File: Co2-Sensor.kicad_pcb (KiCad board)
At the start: 2 copper layers, 45 x 65 mm, 74 parts, among them J1 OLED, J2 SCD30, J3 LED, J4 Power, J5 USB_C_Receptacle_USB2.0, J6 LED, J7 SPS30, J8 I2C, Q1 S8050, Q2 S8050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

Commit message: Add changes for Rev. 2
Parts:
- removed D7: Red, LED_SMD:LED_0603_1608Metric
- removed R21: 0R NC, Resistor_SMD:R_0603_1608Metric
- removed R22: 0R, Resistor_SMD:R_0603_1608Metric
- added Q4: 2N7002, Package_TO_SOT_SMD:SOT-23, F.Cu at (163.0, 112.5)
- added REF**: MountingHole_JLCPCB, MountingHole:MountingHole_JLCPCB, F.Cu at (171.0, 128.0)
- added REF**: MountingHole_JLCPCB, MountingHole:MountingHole_JLCPCB, F.Cu at (129.0, 128.0)
- added REF**: MountingHole_JLCPCB, MountingHole:MountingHole_JLCPCB, F.Cu at (129.0, 75.0)
- added REF**: MountingHole_JLCPCB, MountingHole:MountingHole_JLCPCB, F.Cu at (171.2, 75.0)
- added TP1: 5V, TestPoint:TestPoint_Pad_2.5x2.5mm, B.Cu at (130.0, 116.0)
- added TP2: 5V, TestPoint:TestPoint_Pad_2.5x2.5mm, B.Cu at (170.0, 116.0)
- added TP3: LED1_CLK, TestPoint:TestPoint_Pad_2.5x2.5mm, B.Cu at (134.0, 116.0)
- added TP4: LED1_DATA, TestPoint:TestPoint_Pad_2.5x2.5mm, B.Cu at (138.0, 116.0)
- added TP5: LED2_CLK, TestPoint:TestPoint_Pad_2.5x2.5mm, B.Cu at (162.0, 116.0)
- added TP6: LED2_DATA, TestPoint:TestPoint_Pad_2.5x2.5mm, B.Cu at (166.0, 116.0)
- added TP7: GND, TestPoint:TestPoint_Pad_2.5x2.5mm, B.Cu at (142.0, 116.0)
- added TP8: GND, TestPoint:TestPoint_Pad_2.5x2.5mm, B.Cu at (158.0, 116.0)
- C1, C4: value 100u/6.3V -> 22u/25V; footprint Capacitor_Tantalum_SMD:CP_EIA-3528-15_AVX-H -> Capacitor_SMD:C_0805_2012Metric
- C7: value 1u/50V -> 2u2/16V
- F1: value 1A -> SMD1210-050; footprint Fuse:Fuse_0805_2012Metric -> Fuse:Fuse_1210_3225Metric
- R16: value 22R -> 4k7
- R18: value 47R -> 15k
- R19: value 330R -> 1k5
- R20: value 470R -> 12k
- R26, R6: value 470R -> 0R
- moved C1 52.2 mm to (129.2, 119.2), turned to 0 degrees
- moved R20 26.6 mm to (166.0, 112.5), turned to 270 degrees
- moved C9 7.38 mm to (130.2, 116.2), turned to 90 degrees
- moved C7 3.95 mm to (138.0, 80.2), turned to 0 degrees
- moved F1 2.69 mm to (142.0, 123.8)
- moved C4 1.02 mm to (137.9, 78.0), turned to 0 degrees
- moved R11 0.75 mm to (153.8, 124.8), turned to 0 degrees
- moved D3 0.63 mm to (150.0, 123.5)
- moved R12 0.45 mm to (146.8, 124.0)
- turned C3 to 270 degrees
- turned C5 to 270 degrees
- turned C8 to 270 degrees
- turned R13 to 270 degrees
- turned R14 to 0 degrees
- turned R15 to 0 degrees
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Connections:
- net /IO0 renamed /BUTTON4
- net /IO15 renamed /BUTTON3
- C1 pad 1: Net-(C1-Pad1) -> /5V_PREFUSE
- C3 pad 1: +5V -> GND
- C3 pad 2: GND -> +5V
- C4 pad 1: +3V3 -> GND
- C4 pad 2: GND -> +3V3
- C5 pad 1: GND -> +5V
- C5 pad 2: +5V -> GND
- C7 pad 1: /EN -> GND
- C7 pad 2: GND -> /EN
- C8 pad 1: GND -> +5V
- C8 pad 2: +5V -> GND
- D1 pad 1: GND -> Net-(D1-Pad1)
- D2 pad 1: Net-(D2-Pad1) -> /5V_PREFUSE
- D4 pad 1: GND -> Net-(D1-Pad1)
- D6 pad 1: Net-(D2-Pad1) -> /5V_PREFUSE
- F1 pad 2: Net-(D2-Pad1) -> /5V_PREFUSE
- J3 pad 2: Net-(C1-Pad1) -> /5V_PREFUSE
- J6 pad 2: Net-(C1-Pad1) -> /5V_PREFUSE
- R1 pad 1: /IO12 -> /BUTTON1
- R11 pad 1: GND -> Net-(J5-PadB5)
- R11 pad 2: Net-(J5-PadB5) -> GND
- R13 pad 1: Net-(R13-Pad1) -> /VBUS
- R13 pad 2: /VBUS -> Net-(R13-Pad2)
- R14 pad 1: GND -> Net-(R13-Pad2)
- R14 pad 2: Net-(R13-Pad1) -> GND
- R15 pad 1: Net-(C2-Pad2) -> Net-(R15-Pad1)
- R15 pad 2: Net-(R15-Pad2) -> Net-(C2-Pad2)
- R16 pad 1: Net-(D1-Pad2) -> +3V3
- R16 pad 2: +3V3 -> Net-(D1-Pad2)
- R18 pad 1: Net-(D4-Pad2) -> +5V
- R18 pad 2: +5V -> Net-(D4-Pad2)
- R19 pad 1: Net-(D5-Pad2) -> /IO2
- R19 pad 2: /IO2 -> Net-(D5-Pad2)
- R2 pad 2: /IO12 -> /BUTTON1
- R20 pad 1: +5V -> +3V3
- R20 pad 2: Net-(D7-Pad2) -> /LED_DISABLE
- R26 pad 1: Net-(Q3-Pad3) -> /EN
- R26 pad 2: /EN -> Net-(Q3-Pad3)
- R29 pad 1: /SPS30_RX -> Net-(J7-Pad2)
- R29 pad 2: Net-(J7-Pad2) -> /SPS30_RX
- R3 pad 1: /IO13 -> /BUTTON2
- R31 pad 1: /SPS30_TX -> Net-(J7-Pad3)
- R31 pad 2: Net-(J7-Pad3) -> /SPS30_TX
- R4 pad 2: /IO13 -> /BUTTON2
- R5 pad 1: /TXD0 -> /RXD
- R5 pad 2: /RXD -> /TXD0
- R7 pad 1: /~DTR -> Net-(Q1-Pad1)
- R7 pad 2: Net-(Q1-Pad1) -> /~DTR
- U1 pad 14: /IO12 -> Net-(U1-Pad14)
- U1 pad 16: /IO13 -> Net-(U1-Pad16)
- U1 pad 33: Net-(U1-Pad33) -> /LED_DISABLE
- U1 pad 36: Net-(U1-Pad36) -> /SCL
- U1 pad 37: Net-(U1-Pad37) -> /SDA
- U1 pad 6: /SDA -> /BUTTON1
- U1 pad 7: /SCL -> /BUTTON2
- U3 pad 8: Net-(R13-Pad1) -> Net-(R13-Pad2)
- U3 pad 9: Net-(R15-Pad2) -> Net-(R15-Pad1)
- U5 pad 1: /IO12 -> /BUTTON1
- U5 pad 2: /IO13 -> /BUTTON2
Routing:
- net +5V: track 93.1 -> 17.5 mm, vias 0 -> 2
- net /LED1_CLK: track 13.8 -> 70.3 mm, vias 0 -> 2
- net /BUTTON1: track 0.00 -> 55.7 mm, vias 0 -> 2
- net /BUTTON2: track 0.00 -> 48.4 mm, vias 0 -> 2
- net /IO12: track 47.5 -> 0.00 mm, vias 2 -> 0
- net /LED1_DATA: track 12.5 -> 56.1 mm, vias 0 -> 2
- net /5V_PREFUSE: track 0.00 -> 42.8 mm, vias 0 -> 6
- net /LED_DISABLE: track 0.00 -> 39.7 mm, vias 0 -> 2
- net /IO13: track 38.1 -> 0.00 mm, vias 2 -> 0
- net /LED2_CLK: track 4.11 -> 33.2 mm
- net /LED2_DATA: track 5.16 -> 33.3 mm, vias 0 -> 1
- net Net-(C1-Pad1): track 26.8 -> 0.00 mm
- net Net-(D1-Pad1): track 0.00 -> 22.2 mm, vias 0 -> 2
- net /SDA: track 60.9 -> 77.4 mm, vias 0 -> 4
- net GND: track 243.2 -> 227.3 mm, vias 52 -> 69
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- added copper zone on F.Cu, net /5V_PREFUSE
- added copper zone on F.Cu, net GND
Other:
- board text added: "CO2 Sensor Board 2020-09-13, Rev. 2 (c) Tobias Müller, Fabian Amann"
- board text added: "LED1_CLK"
- board text added: "LED1_DATA"
- board text added: "LED2_CLK"
- board text added: "LED2_DATA"
- board text removed: "CO2 Sensor Board 2020-09-13, Rev. 1 (c) Tobias Müller, Fabian Amann"

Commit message: Minor improvements
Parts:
- removed R2, R24, R28, R4: 470R, Resistor_SMD:R_0603_1608Metric
- removed R26: 0R, Resistor_SMD:R_0603_1608Metric
- added C10: 100n/50V, Capacitor_SMD:C_0603_1608Metric, F.Cu at (140.0, 116.5)
- added C11: 100n/50V, Capacitor_SMD:C_0603_1608Metric, F.Cu at (150.0, 116.5)
- added C12: 100n/50V, Capacitor_SMD:C_0603_1608Metric, F.Cu at (160.0, 116.5)
- added C13: 100n/50V, Capacitor_SMD:C_0603_1608Metric, F.Cu at (170.0, 116.5)
- R1, R23, R25, R27, R3, R7, R8: value 12k -> 10k
- moved Q2 2.75 mm to (166.2, 106.8)
- moved R7 2.72 mm to (166.3, 109.2)
- moved R8 2.51 mm to (162.5, 109.2)
- moved Q1 2.50 mm to (162.5, 106.8)
- moved R25 2.25 mm to (159.8, 106.8)
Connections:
- Q3 pad 3: Net-(Q3-Pad3) -> /EN
- SW1 pad 1: Net-(R2-Pad1) -> /BUTTON1
- SW2 pad 1: Net-(R4-Pad1) -> /BUTTON2
- SW3 pad 1: Net-(R24-Pad1) -> /BUTTON3
- SW4 pad 1: Net-(R28-Pad1) -> /BUTTON4
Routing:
- net /BUTTON4: track 43.2 -> 53.5 mm
- net /BUTTON1: track 55.7 -> 64.6 mm
- net /BUTTON2: track 48.4 -> 57.3 mm
- net Net-(R4-Pad1): track 8.17 -> 0.00 mm
- net Net-(R28-Pad1): track 8.17 -> 0.00 mm
- net Net-(R24-Pad1): track 8.17 -> 0.00 mm
- net Net-(R2-Pad1): track 8.17 -> 0.00 mm
- net GND: track 227.3 -> 235.3 mm, vias 69 -> 73
- net Net-(Q3-Pad3): track 3.74 -> 0.00 mm
- net +3V3: track 77.8 -> 75.4 mm
- net /EN: track 51.8 -> 53.9 mm
- net /~DTR: track 30.0 -> 28.1 mm
- net Net-(Q2-Pad1): track 3.72 -> 2.58 mm
- net /~RTS: track 31.8 -> 31.7 mm, vias 3 -> 2

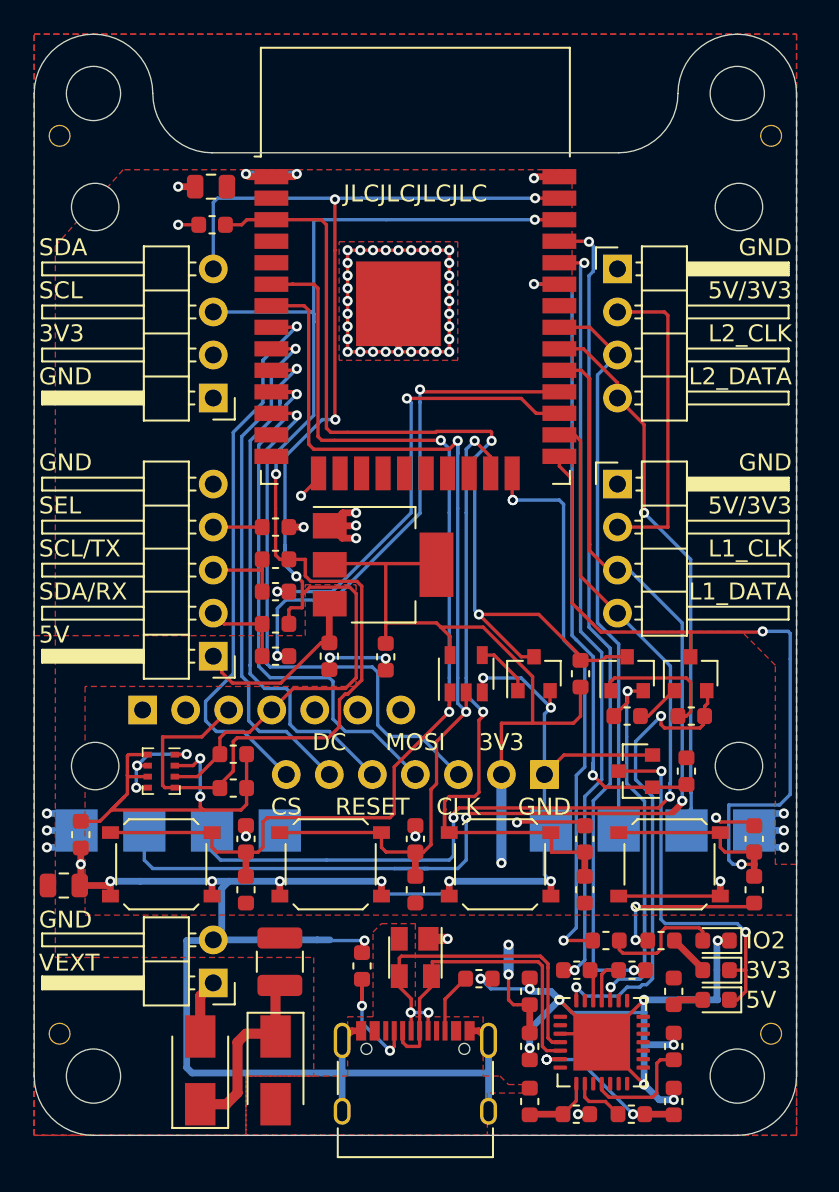
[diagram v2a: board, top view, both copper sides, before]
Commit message: Add more capacitance to ESP
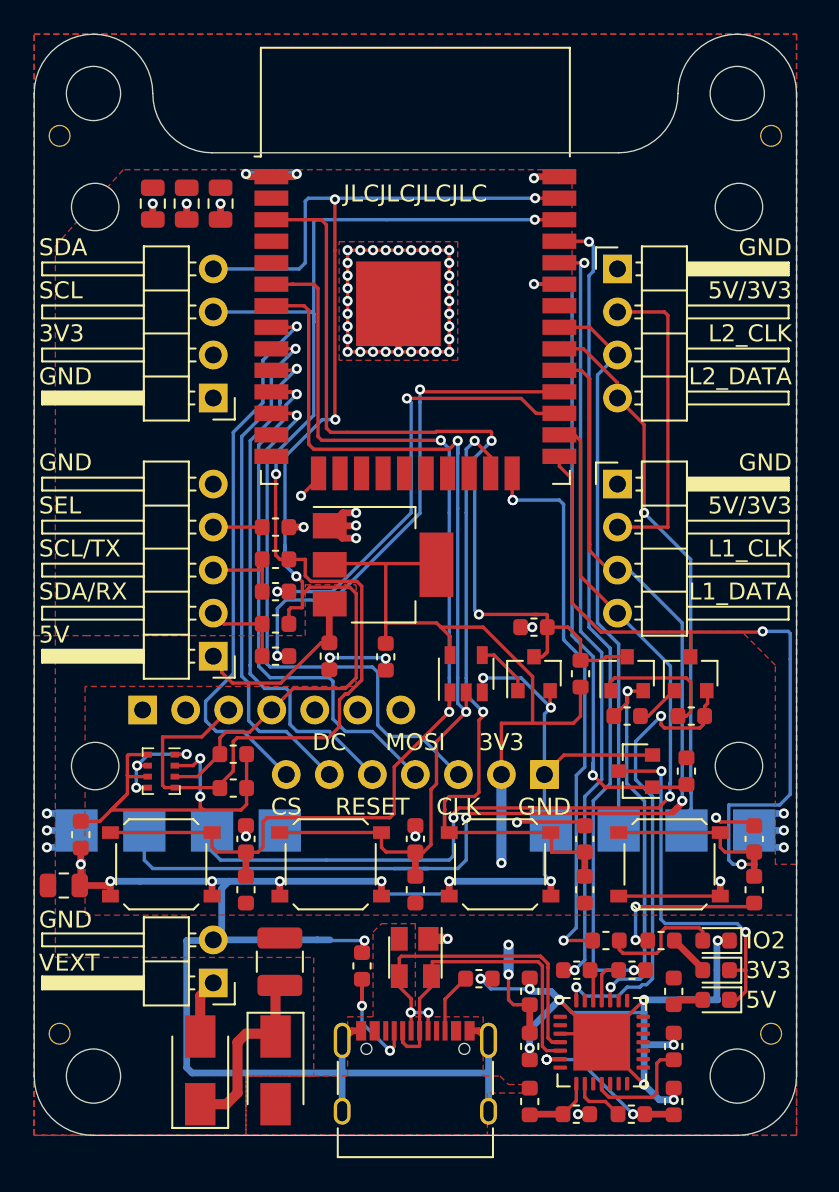
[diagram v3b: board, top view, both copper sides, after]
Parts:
- added C14: 22u/25V, Capacitor_SMD:C_0805_2012Metric, F.Cu at (134.5, 79.0)
- added C15: 22u/25V, Capacitor_SMD:C_0805_2012Metric, F.Cu at (136.5, 79.0)
- moved C7 30.4 mm to (157.0, 104.0)
- moved C4 1.15 mm to (138.5, 79.0), turned to 90 degrees
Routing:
- net /EN: track 53.9 -> 50.8 mm
- net GND: track 235.3 -> 236.6 mm, vias 73 -> 75

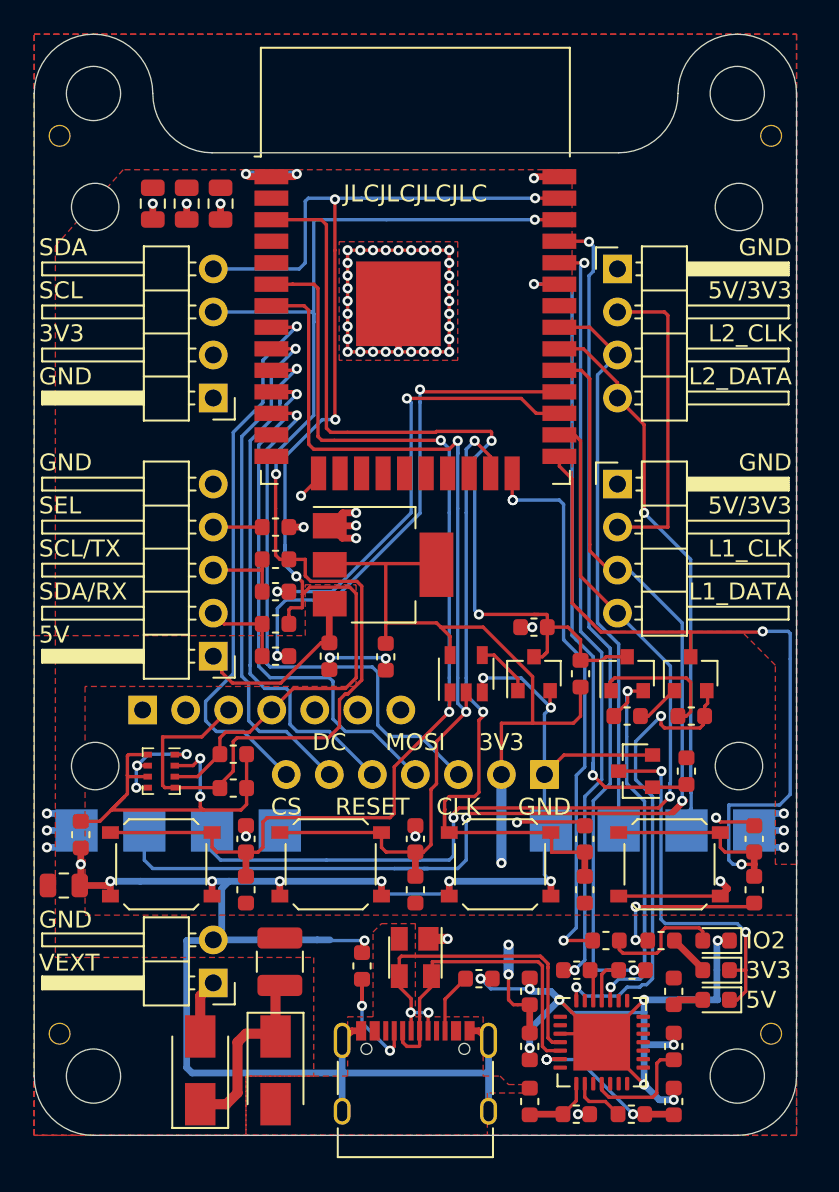
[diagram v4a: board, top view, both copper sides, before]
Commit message: Update to KiCad 6
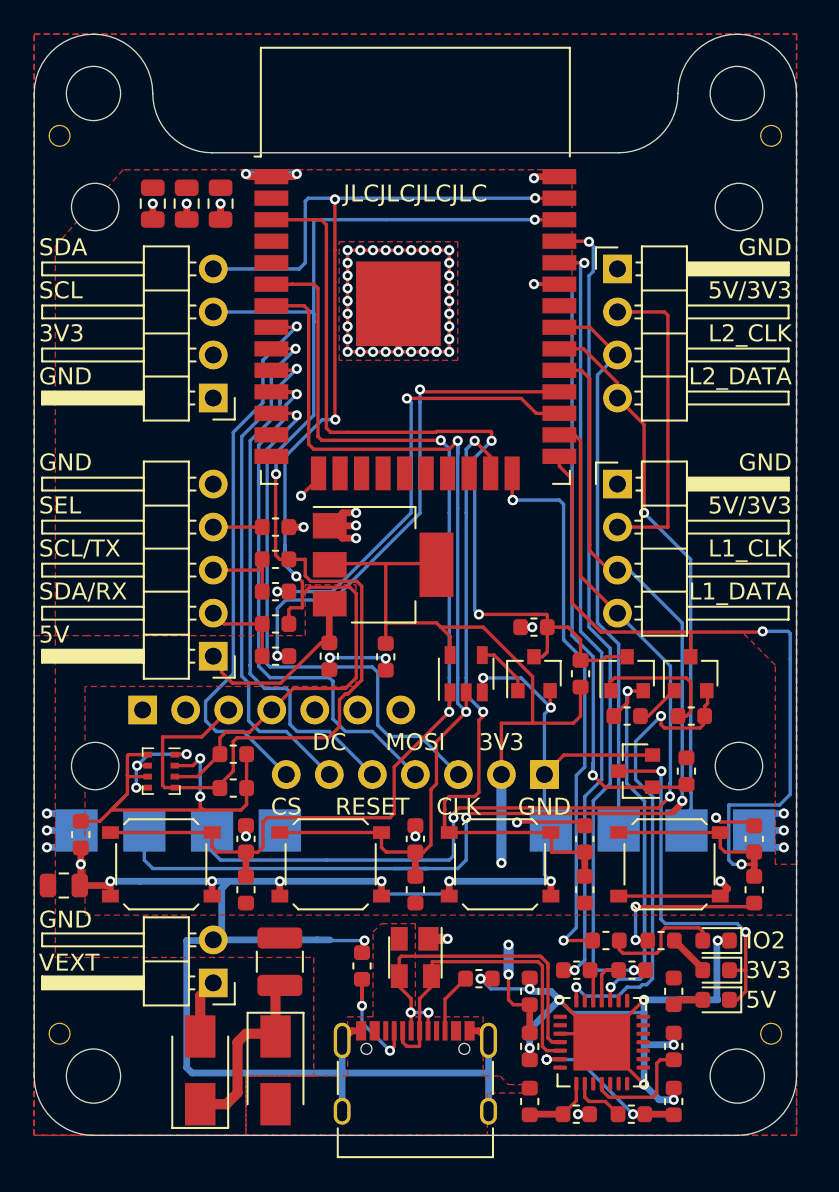
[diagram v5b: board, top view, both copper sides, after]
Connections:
- net /~DTR renamed /~{DTR}
- net /~RTS renamed /~{RTS}
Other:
- net class Default removed
